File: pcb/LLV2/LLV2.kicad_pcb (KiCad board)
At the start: 2 copper layers, 1 part, among them U1 XIAO-nRF52840-SMD

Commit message: Begin drafting final PCB layout
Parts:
- added J1: Conn_01x02, Connector_PinHeader_2.54mm:PinHeader_1x02_P2.54mm_Vertical_SMD_Pin1Right, F.Cu at (122.8, 96.0)
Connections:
- U1 pad 12: unconnected-(U1-3V3_OUT-Pad12) -> +3V3
- U1 pad 13: unconnected-(U1-GND-Pad13) -> GND
- U1 pad 18: unconnected-(U1-GND-Pad18) -> GND
- U1 pad 19: unconnected-(U1-VBAT-Pad19) -> Net-(J1-Pin_1)
- U1 pad 20: unconnected-(U1-GND-Pad20) -> GND

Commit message: PCBV2 updates 10/12
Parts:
- added BZ1: Buzzer, Package_SO:SOIC-8_3.9x4.9mm_P1.27mm, F.Cu at (130.7, 132.7)
- added D1: 1N4148W, Diode_SMD:D_SOD-123, F.Cu at (146.8, 131.0)
- added D2: 1N4148W, Diode_SMD:D_SOD-123, F.Cu at (146.8, 134.3)
- added Q1: AO3400A, Package_TO_SOT_SMD:SOT-23, F.Cu at (141.4, 131.5)
- added Q2: AO3400A, Package_TO_SOT_SMD:SOT-23, F.Cu at (141.4, 136.0)
- added R1: 1K, Resistor_SMD:R_0603_1608Metric, F.Cu at (137.0, 130.6)
- added R2: 100K, Resistor_SMD:R_0603_1608Metric, F.Cu at (137.0, 133.1)
- added R3: 1K, Resistor_SMD:R_0603_1608Metric, F.Cu at (137.0, 135.6)
- added R4: 100K, Resistor_SMD:R_0603_1608Metric, F.Cu at (137.0, 138.1)
- added SW1: SW_Push, Package_SO:SOIC-8_3.9x4.9mm_P1.27mm, F.Cu at (130.7, 139.2)
- added U2: MAX30102, MAX30102SMD:MAX30102_SMD, B.Cu at (136.6, 101.3)
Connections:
- U1 pad 2: unconnected-(U1-D1-Pad2) -> Net-(U1-D1)
- U1 pad 3: unconnected-(U1-D2-Pad3) -> Net-(U1-D2)
- U1 pad 4: unconnected-(U1-D3-Pad4) -> Net-(U1-D3)
- U1 pad 5: unconnected-(U1-D4-Pad5) -> Net-(U1-D4)
- U1 pad 6: unconnected-(U1-D5-Pad6) -> Net-(U1-D5)

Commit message: PCBV2 edits
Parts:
- SW1: footprint Package_SO:SOIC-8_3.9x4.9mm_P1.27mm -> easyeda2kicad:KEY-SMD_4P-L4.8-W4.6-P1.70-LS6.2
- moved U2 67.6 mm to (75.5, 72.6)
- moved SW1 59.6 mm to (173.4, 97.8), turned to 90 degrees
- moved BZ1 47.8 mm to (118.5, 86.4)
- moved D2 42.4 mm to (129.2, 95.8)
- moved J1 37.7 mm to (156.6, 112.5)
- moved D1 37.6 mm to (118.7, 106.0)
- moved R4 34.5 mm to (130.3, 104.2)
- moved R3 31.7 mm to (139.6, 104.0)
- moved Q2 18.1 mm to (136.6, 118.5)
- moved Q1 18.1 mm to (159.2, 128.0)
- moved U1 16.5 mm to (143.0, 105.9)

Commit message: PCBV2 updates 10/20
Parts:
- moved U2 88.3 mm to (160.8, 95.2), turned to 90 degrees
- moved D1 68.8 mm to (183.2, 130.0)
- moved R1 51.4 mm to (187.3, 141.1)
- moved R2 51.4 mm to (187.3, 143.6)
- moved Q1 51.4 mm to (209.5, 138.4)
- moved SW1 37.2 mm to (140.8, 115.6)
- moved BZ1 34.4 mm to (114.8, 52.2)
- moved D2 34.4 mm to (125.6, 61.5)
- moved Q2 34.4 mm to (132.9, 84.2)
- moved R3 34.4 mm to (135.9, 69.8)
- moved R4 34.4 mm to (126.7, 70.0)
- moved J1 33.0 mm to (189.5, 109.5)
- moved U1 4.28 mm to (147.2, 104.9)
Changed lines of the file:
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@@
 	(footprint "Seeed_Studio_XIAO_Series:XIAO-nRF52840-SMD"
 		(layer "F.Cu")
-		(at 143 105.87)
+		(at 147.165 104.88)
 		(property "Reference" "U1"
 			(at 7.112 -21.336 0)
@@
 	(footprint "Package_TO_SOT_SMD:SOT-23"
 		(layer "F.Cu")
-		(at 136.5625 118.5)
+		(at 132.9125 84.25)
 		(descr "SOT, 3 Pin (JEDEC TO-236 Var AB https://www.jedec.org/document_search?search_api_views_fulltext=TO-236)")
 		(tags "SOT TO_SOT_SMD")
@@
 	(footprint "Diode_SMD:D_SOD-123"
 		(layer "F.Cu")
-		(at 129.25 95.75)
+		(at 125.6 61.5)
 		(descr "SOD-123")
 		(tags "SOD-123")
@@
 	(footprint "Resistor_SMD:R_0603_1608Metric"
 		(layer "F.Cu")
-		(at 136.955 130.555)
+		(at 187.305 141.055)
 		(descr "Resistor SMD 0603 (1608 Metric), square (rectangular) end terminal, IPC-7351 nominal, (Body size source: IPC-SM-782 page 72, https://www.pcb-3d.com/wordpress/wp-content/uploads/ipc-sm-782a_amendment_1_and_2.pdf)")
 		(tags "resistor")
@@
 	(footprint "Resistor_SMD:R_0603_1608Metric"
 		(layer "F.Cu")
-		(at 139.575 104)
+		(at 135.925 69.75)
 		(descr "Resistor SMD 0603 (1608 Metric), square (rectangular) end terminal, IPC-7351 nominal, (Body size source: IPC-SM-782 page 72, https://www.pcb-3d.com/wordpress/wp-content/uploads/ipc-sm-782a_amendment_1_and_2.pdf)")
 		(tags "resistor")
@@
 	(footprint "Connector_PinHeader_2.54mm:PinHeader_1x02_P2.54mm_Vertical_SMD_Pin1Right"
 		(layer "F.Cu")
-		(at 156.595 112.52)
+		(at 189.5 109.5)
 		(descr "surface-mounted straight pin header, 1x02, 2.54mm pitch, single row, style 2 (pin 1 right)")
 		(tags "Surface mounted pin header SMD 1x02 2.54mm single row style2 pin1 right")
@@
 	(footprint "Package_SO:SOIC-8_3.9x4.9mm_P1.27mm"
 		(layer "F.Cu")
-		(at 118.475 86.405)
+		(at 114.825 52.155)
 		(descr "SOIC, 8 Pin (JEDEC MS-012AA, https://www.analog.com/media/en/package-pcb-resources/package/pkg_pdf/soic_narrow-r/r_8.pdf)")
 		(tags "SOIC SO")
@@
 	(footprint "Resistor_SMD:R_0603_1608Metric"
 		(layer "F.Cu")
-		(at 130.325 104.25)
+		(at 126.675 70)
 		(descr "Resistor SMD 0603 (1608 Metric), square (rectangular) end terminal, IPC-7351 nominal, (Body size source: IPC-SM-782 page 72, https://www.pcb-3d.com/wordpress/wp-content/uploads/ipc-sm-782a_amendment_1_and_2.pdf)")
 		(tags "resistor")
@@
 	(footprint "Resistor_SMD:R_0603_1608Metric"
 		(layer "F.Cu")
-		(at 136.955 133.065)
+		(at 187.305 143.565)
 		(descr "Resistor SMD 0603 (1608 Metric), square (rectangular) end terminal, IPC-7351 nominal, (Body size source: IPC-SM-782 page 72, https://www.pcb-3d.com/wordpress/wp-content/uploads/ipc-sm-782a_amendment_1_and_2.pdf)")
 		(tags "resistor")
@@
 	(footprint "Package_TO_SOT_SMD:SOT-23"
 		(layer "F.Cu")
-		(at 159.1875 127.95)
+		(at 209.5375 138.45)
 		(descr "SOT, 3 Pin (JEDEC TO-236 Var AB https://www.jedec.org/document_search?search_api_views_fulltext=TO-236)")
 		(tags "SOT TO_SOT_SMD")
@@
 	(footprint "easyeda2kicad:KEY-SMD_4P-L4.8-W4.6-P1.70-LS6.2"
 		(layer "F.Cu")
-		(at 173.45 97.75 90)
+		(at 140.85 115.6 90)
 		(property "Reference" "SW1"
 			(at 0 -4.85 90)
@@
 			)
 		)
-		(property "LCSC Part" "C136662"
-			(at 0 0 90)
-			(layer "F.Fab")
-			(hide yes)
-			(effects
-				(font
-					(size 1.27 1.27)
-					(thickness 0.15)
-				)
-			)
-		)
 		(sheetname "/")
 		(sheetfile "LLV2.kicad_sch")
@@
 	(footprint "Diode_SMD:D_SOD-123"
 		(layer "F.Cu")
-		(at 118.65 106)
+		(at 183.15 130)
 		(descr "SOD-123")
 		(tags "SOD-123")
@@
 	(footprint "MAX30102SMD:MAX30102_SMD"
 		(layer "B.Cu")
-		(at 75.465 72.58 -90)
+		(at 160.782 95.25 90)
 		(property "Reference" "U2"
-			(at 0 0.5 90)
+			(at 0 0.5 270)
 			(unlocked yes)
 			(layer "B.SilkS")
@@
 		)
 		(property "Value" "MAX30102"
-			(at 0 -1 90)
+			(at 0 -1 270)
 			(unlocked yes)
 			(layer "B.Fab")
@@
 		)
 		(property "Datasheet" "https://datasheets.maximintegrated.com/en/ds/MAX30102.pdf"
-			(at 0 0 90)
+			(at 0 0 270)
 			(unlocked yes)
 			(layer "B.Fab")
@@
 		)
 		(property "Description" "Heart Rate Sensor, 14-OLGA"
-			(at 0 0 90)
+			(at 0 0 270)
 			(unlocked yes)
 			(layer "B.Fab")
@@
 			(layer "B.SilkS")
 		)
-		(fp_text user "VIN"
-			(at -3.409 2.413 0)
+		(fp_text user "GND"
+			(at 4.211 2.032 180)
 			(unlocked yes)
 			(layer "B.SilkS")
@@
 			)
 		)
-		(fp_text user "SDA"
-			(at -0.869 2.159 0)
+		(fp_text user "SCL"
+			(at 1.671 2.159 180)
 			(unlocked yes)
 			(layer "B.SilkS")
@@
 			)
 		)
-		(fp_text user "SCL"
-			(at 1.671 2.159 0)
+		(fp_text user "SDA"
+			(at -0.869 2.159 180)
 			(unlocked yes)
 			(layer "B.SilkS")
@@
 			)
 		)
-		(fp_text user "GND"
-			(at 4.211 2.032 0)
+		(fp_text user "VIN"
+			(at -3.409 2.413 180)
 			(unlocked yes)
 			(layer "B.SilkS")
@@
 		)
 		(fp_text user "${REFERENCE}"
-			(at 0 -2.5 90)
+			(at 0 -2.5 270)
 			(unlocked yes)
 			(layer "B.Fab")
@@
 		)
 		(pad "2" smd rect
-			(at 1.27 7.62 270)
+			(at 1.27 7.62 90)
 			(size 1.4 1.7)
 			(layers "B.Cu" "B.Mask")
@@
 		)
 		(pad "3" smd rect
-			(at -1.27 7.62 270)
+			(at -1.27 7.62 90)
 			(size 1.4 1.7)
 			(layers "B.Cu" "B.Mask")
@@
 		)
 		(pad "11" smd rect
-			(at -3.81 7.62 270)
+			(at -3.81 7.62 90)
 			(size 1.4 1.7)
 			(layers "B.Cu" "B.Mask")
@@
 		)
 		(pad "12" smd rect
-			(at 3.81 7.62 270)
+			(at 3.81 7.62 90)
 			(size 1.4 1.7)
 			(layers "B.Cu" "B.Mask")
@@
 			(polygon
 				(pts
-					(xy 67.765 62.43) (xy 67.765 82.73) (xy 83.165 82.73) (xy 83.165 62.43)
+					(xy 168.482 105.4) (xy 168.482 85.1) (xy 153.082 85.1) (xy 153.082 105.4)
 				)
 			)

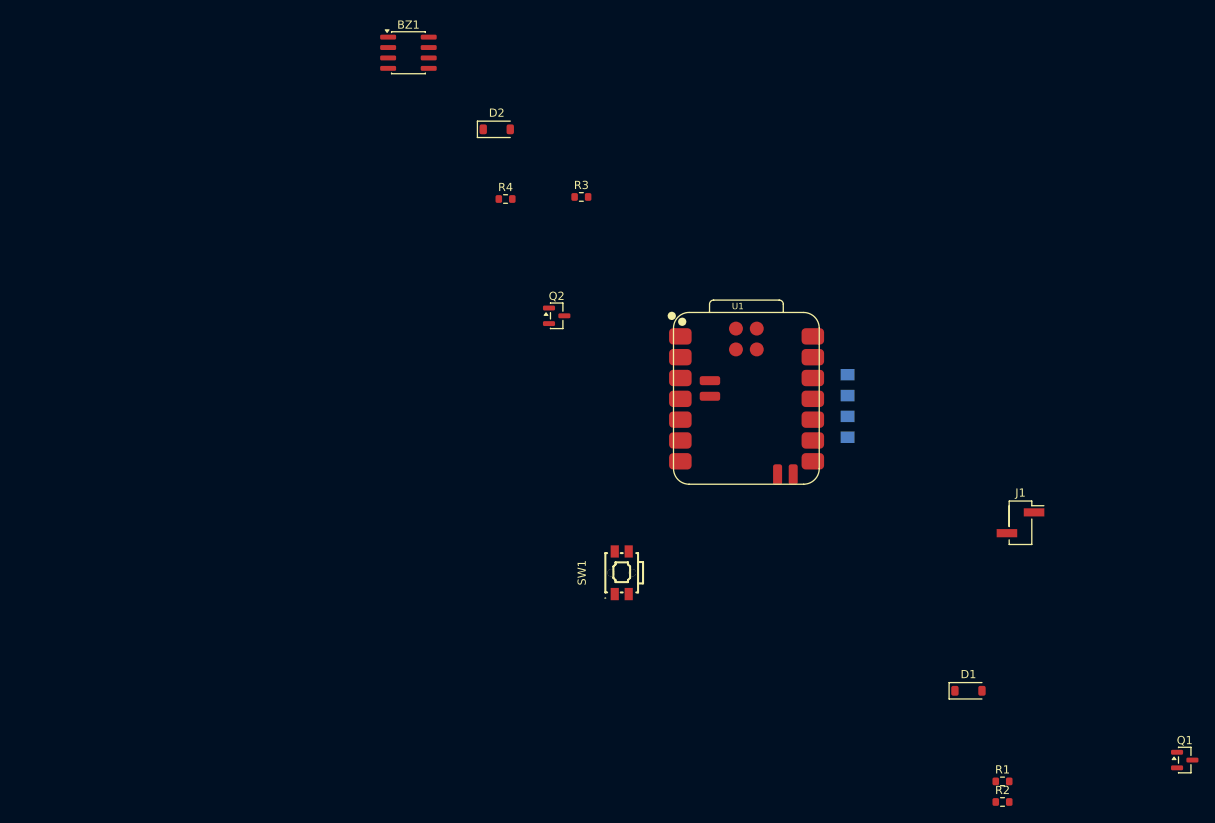
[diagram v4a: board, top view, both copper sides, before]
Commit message: Major PCBV2 edits + Fall Detection Overhaul
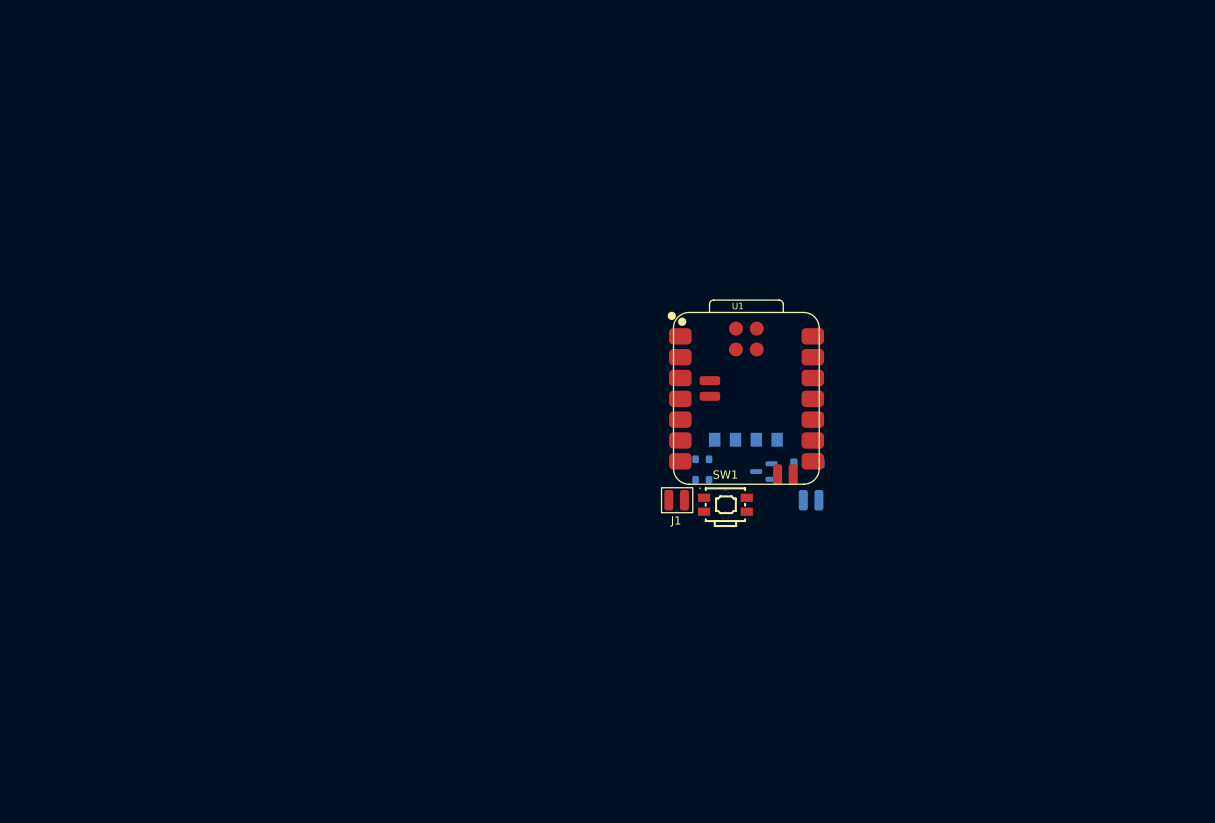
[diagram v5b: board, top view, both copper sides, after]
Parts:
- removed BZ1: Buzzer, Package_SO:SOIC-8_3.9x4.9mm_P1.27mm
- removed D2: 1N4148W, Diode_SMD:D_SOD-123
- removed Q2: AO3400A, Package_TO_SOT_SMD:SOT-23
- removed R3: 1K, Resistor_SMD:R_0603_1608Metric
- removed R4: 100K, Resistor_SMD:R_0603_1608Metric
- added M1: Motor_DC, CustomSolderPads:Battery_Copper_Pads, B.Cu at (164.0, 106.8)
- D1, Q1, R1, R2: moved to B.Cu
- J1: footprint Connector_PinHeader_2.54mm:PinHeader_1x02_P2.54mm_Vertical_SMD_Pin1Right -> CustomSolderPads:Battery_Copper_Pads
- moved Q1 62.3 mm to (158.2, 103.2), turned to 180 degrees
- moved R1 53.7 mm to (150.7, 101.8), turned to 180 degrees
- moved R2 53.7 mm to (150.7, 104.3), turned to 180 degrees
- moved J1 42.1 mm to (147.5, 106.8), turned to 90 degrees
- moved D1 34.0 mm to (163.5, 102.2), turned to 180 degrees
- moved SW1 15.1 mm to (153.5, 107.3), turned to 0 degrees
- moved U2 5.93 mm to (156.0, 91.8), turned to 0 degrees
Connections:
- U1 pad 2: Net-(U1-D1) -> unconnected-(U1-D1-Pad2)

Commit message: PCBV2 updates 10/27
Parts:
- D1: footprint Diode_SMD:D_SOD-123 -> Diode_SMD:D_SOD-323
- R1, R2: footprint Resistor_SMD:R_0603_1608Metric -> Resistor_SMD:R_0402_1005Metric
- moved R2 6.04 mm to (156.7, 104.3)
- moved R1 3.75 mm to (154.4, 101.8)
- moved SW1 2.72 mm to (156.2, 107.5)
- moved Q1 1.67 mm to (158.4, 101.6)
- moved J1 0.72 mm to (148.2, 106.8)
